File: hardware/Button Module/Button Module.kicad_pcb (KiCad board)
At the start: 2 copper layers, 27.9 x 22.9 mm, 10 parts, among them J1 1A, J2 1A, J3 2A, J4 2A, J5 1B, J6 1B, J7 2B, J8 2B, SW1 B3F-4055, SW2 B3F-4055

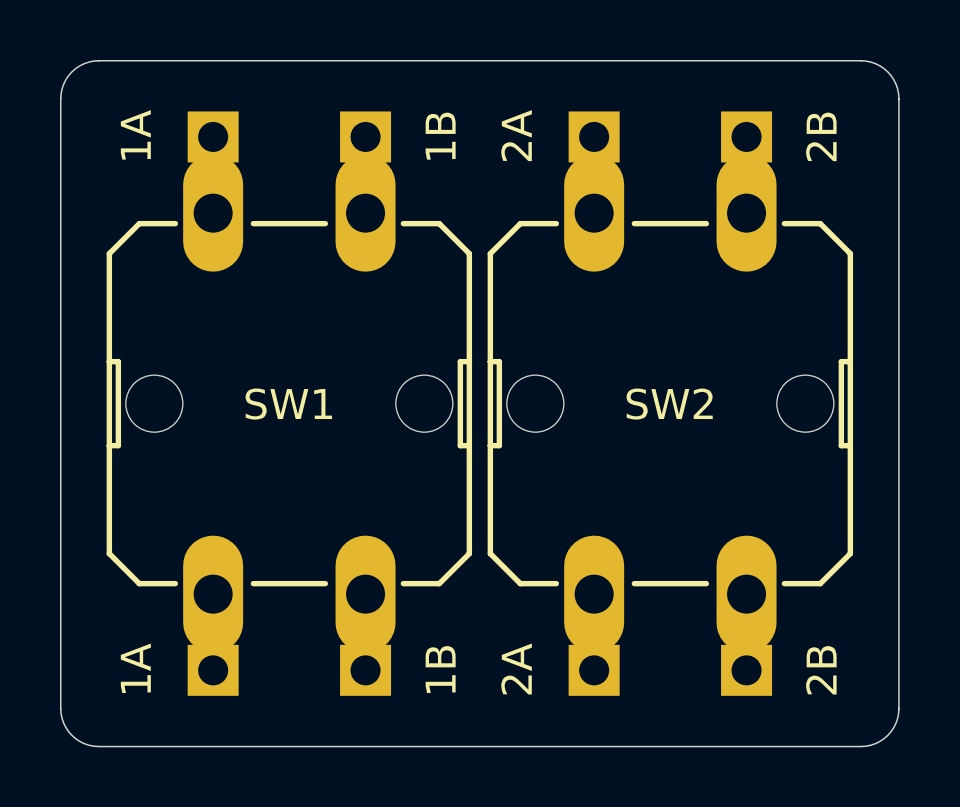
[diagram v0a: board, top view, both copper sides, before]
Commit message: Updated instructions for RPi 4 boards
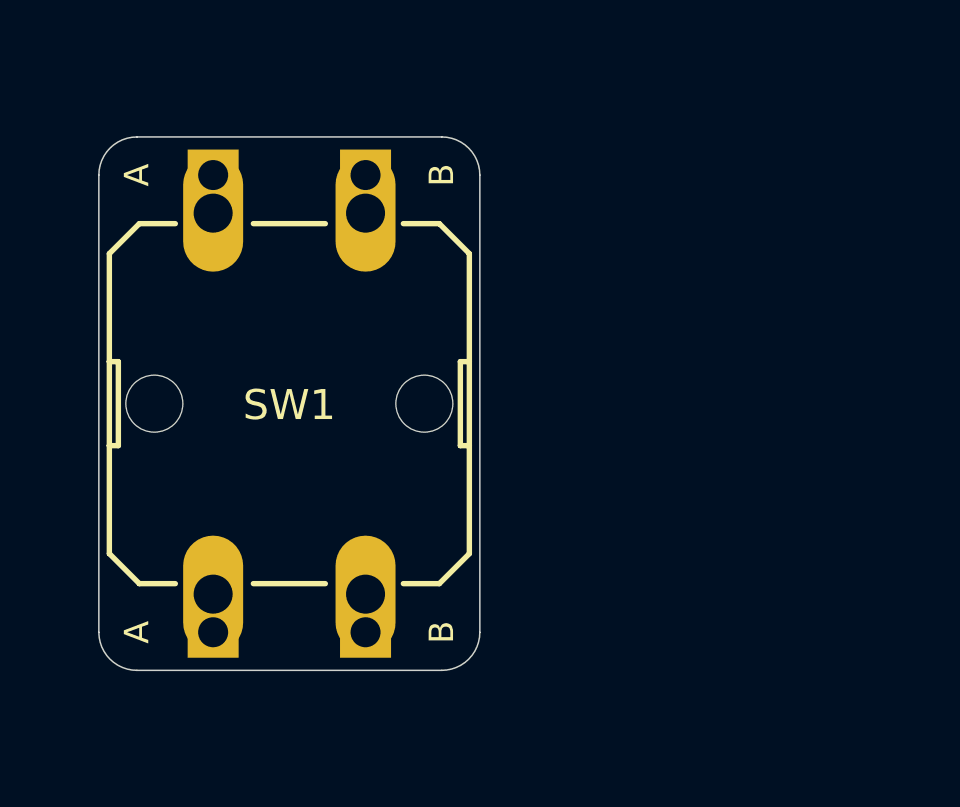
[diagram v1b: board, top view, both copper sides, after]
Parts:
- removed J3, J4: 2A, Connector_PinHeader_2.54mm:PinHeader_1x01_P2.54mm_Vertical
- removed J7, J8: 2B, Connector_PinHeader_2.54mm:PinHeader_1x01_P2.54mm_Vertical
- removed SW2: B3F-4055, switches:B3F-40XX
- J1, J2: value 1A -> A; moved to B.Cu
- J5, J6: value 1B -> B; moved to B.Cu
- moved J1 1.27 mm to (160.0, 85.1), turned to 0 degrees
- moved J2 1.27 mm to (160.0, 69.8), turned to 0 degrees
- moved J5 1.27 mm to (165.1, 85.1)
- moved J6 1.27 mm to (165.1, 69.8)
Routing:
- net Net-(J7-Pad1): track 5.08 -> 0.00 mm
- net Net-(J5-Pad1): track 5.08 -> 0.00 mm
- net Net-(J3-Pad1): track 5.08 -> 0.00 mm
- net Net-(J1-Pad1): track 5.08 -> 0.00 mm
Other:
- board size 27.9 x 22.9 mm -> 12.7 x 17.8 mm
